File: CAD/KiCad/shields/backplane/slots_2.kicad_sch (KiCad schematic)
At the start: 9 parts

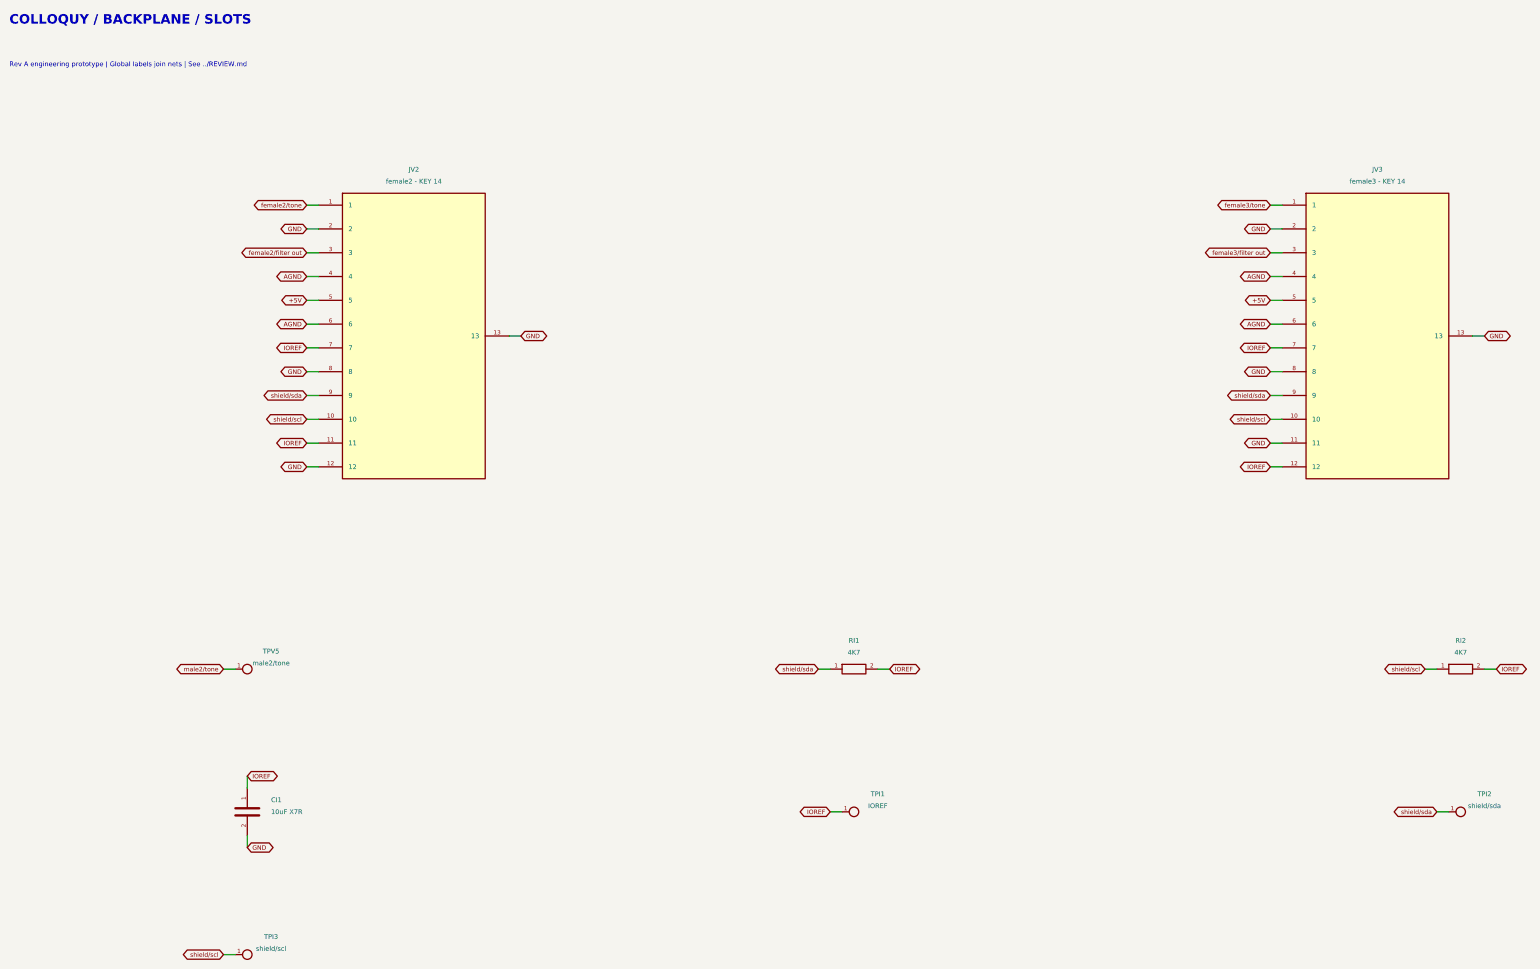
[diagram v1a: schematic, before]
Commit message: Remove shield identification and adopt the simplified connector and Teensy pin maps
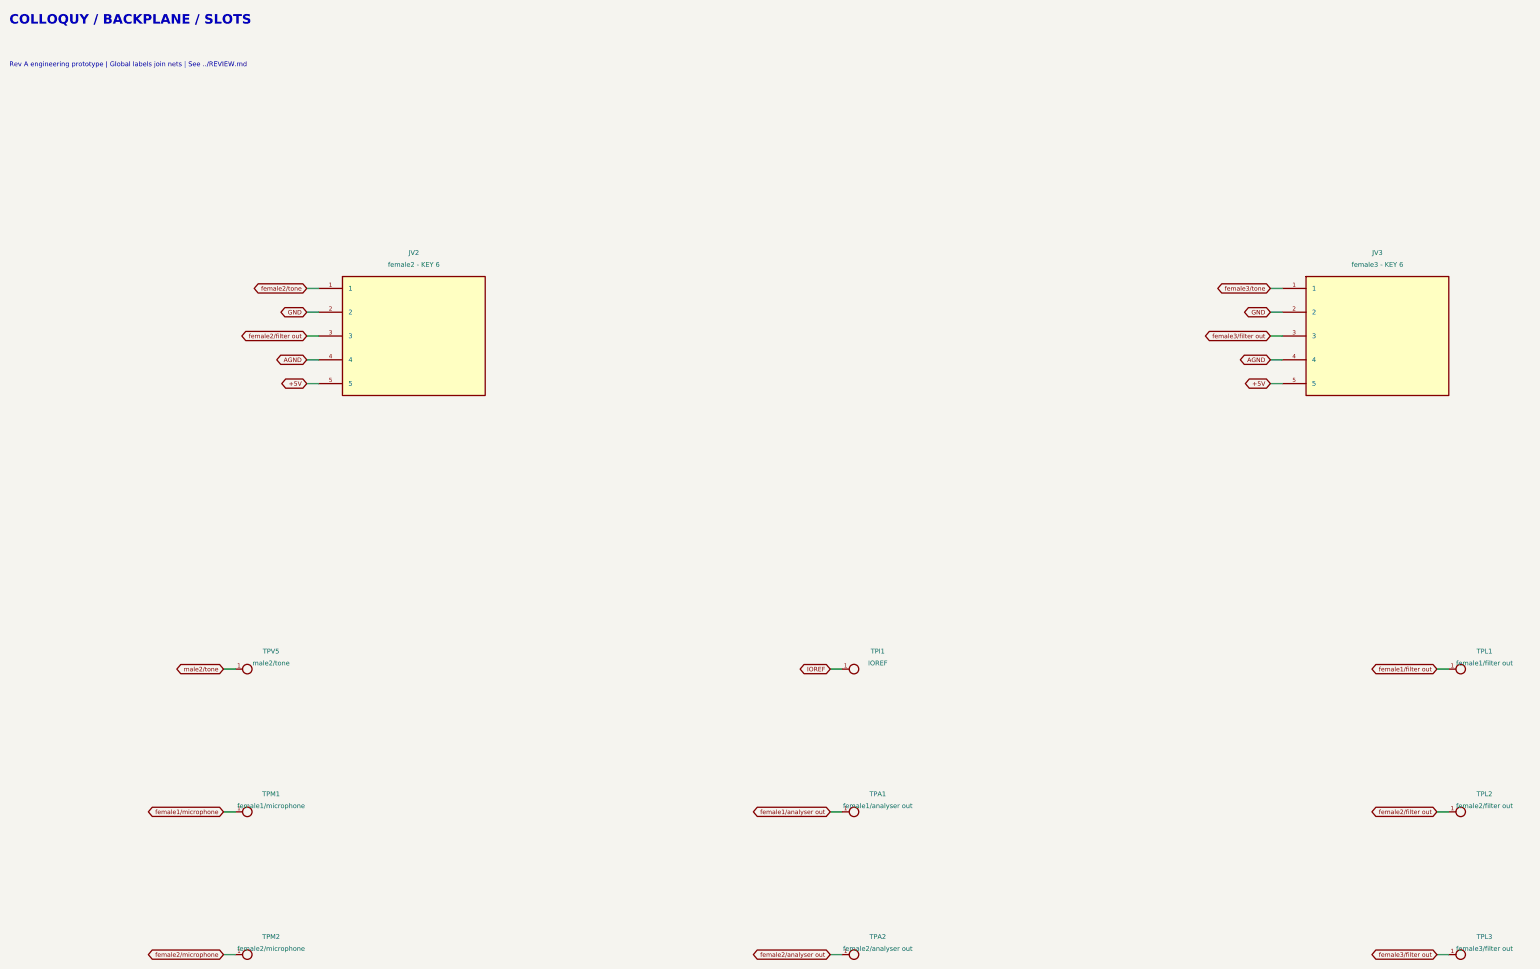
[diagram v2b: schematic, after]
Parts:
- removed CI1: 10uF X7R, Shields:C_0805_2012Metric, symbol Colloquy:CI1
- removed RI1: 4K7, Shields:R_0603_1608Metric, symbol Colloquy:RI1
- removed RI2: 4K7, Shields:R_0603_1608Metric, symbol Colloquy:RI2
- removed TPI2: shield/sda, Shields:TestPoint_Pad_D1.5mm, symbol Colloquy:TPI2
- removed TPI3: shield/scl, Shields:TestPoint_Pad_D1.5mm, symbol Colloquy:TPI3
- added TPA1: female1/analyser out, Shields:TestPoint_Pad_D1.5mm, symbol Colloquy:TPA1
- added TPA2: female2/analyser out, Shields:TestPoint_Pad_D1.5mm, symbol Colloquy:TPA2
- added TPL1: female1/filter out, Shields:TestPoint_Pad_D1.5mm, symbol Colloquy:TPL1
- added TPL2: female2/filter out, Shields:TestPoint_Pad_D1.5mm, symbol Colloquy:TPL2
- added TPL3: female3/filter out, Shields:TestPoint_Pad_D1.5mm, symbol Colloquy:TPL3
- added TPM1: female1/microphone, Shields:TestPoint_Pad_D1.5mm, symbol Colloquy:TPM1
- added TPM2: female2/microphone, Shields:TestPoint_Pad_D1.5mm, symbol Colloquy:TPM2
- JV2: value female2 - KEY 14 -> female2 - KEY 6; footprint Shields:Header_2x07_Key14 -> Shields:Header_2x03_Key6
- JV3: value female3 - KEY 14 -> female3 - KEY 6; footprint Shields:Header_2x07_Key14 -> Shields:Header_2x03_Key6
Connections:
- net AGND: no longer JV2.6, JV3.6
- net GND: no longer JV2.12, JV2.13, JV2.8, JV3.11, JV3.13, JV3.8
- net IOREF: no longer JV2.11, JV2.7, JV3.12, JV3.7
- net female2/filter out: now also TPL2.1
- net female3/filter out: now also TPL3.1
- removed net shield/scl: JV2.10, JV3.10
- removed net shield/sda: JV2.9, JV3.9
- new net female1/analyser out: TPA1.1
- new net female1/filter out: TPL1.1
- new net female1/microphone: TPM1.1
- new net female2/analyser out: TPA2.1
- new net female2/microphone: TPM2.1
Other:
- moved on the sheet: TPI1

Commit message: Route microphones directly to Teensy and remove the analyser buffer board
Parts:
- removed TPI1: IOREF, Shields:TestPoint_Pad_D1.5mm, symbol Colloquy:TPI1
- added TPM3: female3/microphone, Shields:TestPoint_Pad_D1.5mm, symbol Colloquy:TPM3
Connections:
- new net female3/microphone: TPM3.1
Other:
- moved on the sheet: TPA1, TPA2, TPL1, TPL2, TPL3, TPM1, TPM2

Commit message: Update shields for Thomas RC cards, debug headers and body microphones
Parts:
- removed TPA1: female1/analyser out, Shields:TestPoint_Pad_D1.5mm, symbol Colloquy:TPA1
- removed TPA2: female2/analyser out, Shields:TestPoint_Pad_D1.5mm, symbol Colloquy:TPA2
- removed TPL1: female1/filter out, Shields:TestPoint_Pad_D1.5mm, symbol Colloquy:TPL1
- removed TPL2: female2/filter out, Shields:TestPoint_Pad_D1.5mm, symbol Colloquy:TPL2
- removed TPL3: female3/filter out, Shields:TestPoint_Pad_D1.5mm, symbol Colloquy:TPL3
- removed TPM1: female1/microphone, Shields:TestPoint_Pad_D1.5mm, symbol Colloquy:TPM1
- removed TPM2: female2/microphone, Shields:TestPoint_Pad_D1.5mm, symbol Colloquy:TPM2
- removed TPM3: female3/microphone, Shields:TestPoint_Pad_D1.5mm, symbol Colloquy:TPM3
- removed TPV5: male2/tone, Shields:TestPoint_Pad_D1.5mm, symbol Colloquy:TPV5
- added TPM5: male2/microphone, Shields:TestPoint_Pad_D1.5mm, symbol Colloquy:TPM5
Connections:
- new net male2/microphone: TPM5.1
